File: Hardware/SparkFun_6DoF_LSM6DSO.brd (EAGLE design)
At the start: 25.4 x 25.4 mm, 64 parts, among them J1 QWIIC_RIGHT_ANGLE, J2 QWIIC_RIGHT_ANGLE, U1 LSM6DS0

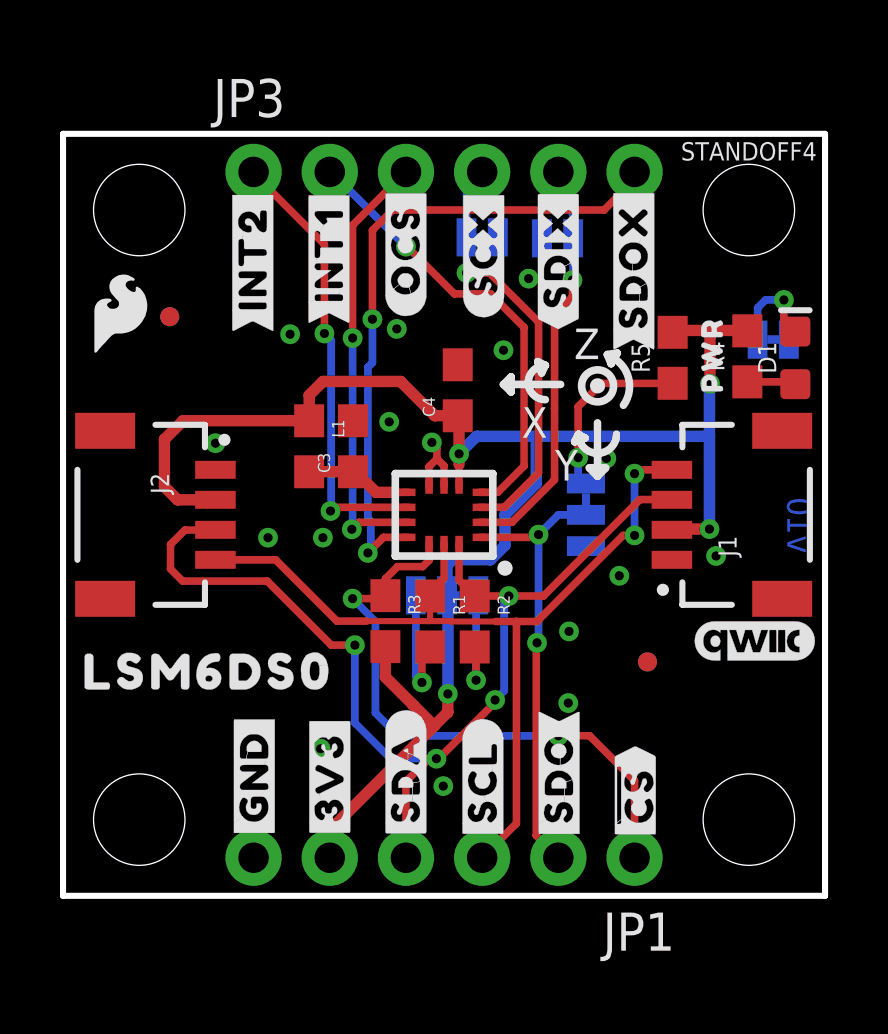
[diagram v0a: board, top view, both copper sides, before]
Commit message: Moves a trace for better ground pour, adds production panel
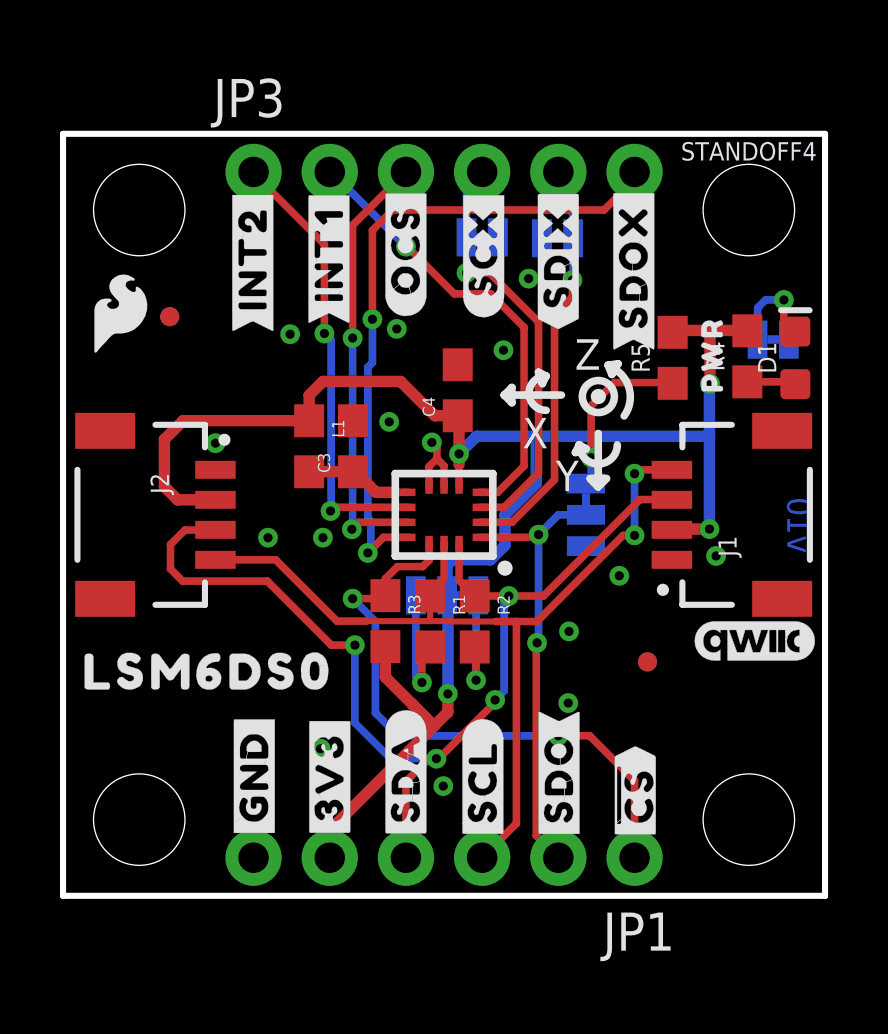
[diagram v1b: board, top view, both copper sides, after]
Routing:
- net GND: vias 16 -> 15
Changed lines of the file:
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@@
 <setting verticaltext="up"/>
 </settings>
-<grid distance="0.05" unitdist="inch" unit="inch" style="dots" multiple="1" display="yes" altdistance="0.005" altunitdist="inch" altunit="inch"/>
+<grid distance="0.01" unitdist="inch" unit="inch" style="dots" multiple="1" display="yes" altdistance="0.001" altunitdist="inch" altunit="inch"/>
 <layers>
 <layer number="1" name="Top" color="4" fill="1" visible="yes" active="yes"/>
@@
 <wire x1="25.4" y1="0" x2="25.4" y2="25.4" width="0.2032" layer="20"/>
 <text x="24.139525" y="11.420475" size="0.8128" layer="16" font="vector" ratio="22" rot="MR90">v10</text>
-<wire x1="14.6812" y1="17.046575" x2="16.5862" y2="17.046575" width="0.254" layer="21"/>
-<wire x1="16.0782" y1="16.538575" x2="16.0782" y2="17.681575" width="0.254" layer="21" curve="-180"/>
-<wire x1="16.0782" y1="17.681575" x2="15.8242" y2="17.808575" width="0.254" layer="21"/>
-<wire x1="16.0782" y1="17.681575" x2="15.9512" y2="17.427575" width="0.254" layer="21"/>
-<wire x1="14.6812" y1="17.046575" x2="14.9352" y2="16.792575" width="0.254" layer="21"/>
-<wire x1="14.6812" y1="17.046575" x2="14.9352" y2="17.300575" width="0.254" layer="21"/>
-<wire x1="17.814925" y1="13.98905" x2="17.814925" y2="15.76705" width="0.254" layer="21"/>
-<wire x1="18.449925" y1="15.38605" x2="17.179925" y2="15.38605" width="0.254" layer="21" curve="-180"/>
-<wire x1="17.179925" y1="15.38605" x2="17.052925" y2="15.13205" width="0.254" layer="21"/>
-<wire x1="17.179925" y1="15.38605" x2="17.408525" y2="15.25905" width="0.254" layer="21"/>
-<wire x1="17.814925" y1="13.98905" x2="18.068925" y2="14.24305" width="0.254" layer="21"/>
-<wire x1="17.814925" y1="13.98905" x2="17.560925" y2="14.24305" width="0.254" layer="21"/>
-<wire x1="18.094325" y1="14.26845" x2="17.535525" y2="14.26845" width="0.254" layer="21"/>
-<wire x1="17.408525" y1="15.25905" x2="17.052925" y2="15.13205" width="0.254" layer="21"/>
-<wire x1="15.8242" y1="17.808575" x2="15.9512" y2="17.427575" width="0.254" layer="21"/>
-<wire x1="14.9352" y1="17.300575" x2="14.9352" y2="16.792575" width="0.254" layer="21"/>
-<text x="16.398875" y="13.843" size="1.016" layer="21" font="vector" ratio="15" rot="SR0">Y</text>
-<text x="15.287625" y="15.27175" size="1.016" layer="21" font="vector" ratio="15" rot="SR0">X</text>
-<text x="17.033875" y="17.891125" size="1.016" layer="21" font="vector" ratio="15" rot="SR0">Z</text>
-<wire x1="18.14195" y1="18.043525" x2="18.475325" y2="18.09115" width="0.254" layer="21"/>
-<wire x1="18.14195" y1="18.043525" x2="18.26895" y2="17.73555" width="0.254" layer="21"/>
-<wire x1="18.26895" y1="17.73555" x2="18.475325" y2="18.09115" width="0.254" layer="21"/>
-<wire x1="18.272125" y1="17.96415" x2="18.678525" y2="16.35125" width="0.254" layer="21" curve="-100"/>
-<circle x="17.8181" y="16.99895" radius="0.127" width="0.254" layer="21"/>
-<circle x="17.8181" y="16.99895" radius="0.5334" width="0.254" layer="21"/>
+<wire x1="14.7066" y1="16.690975" x2="16.6116" y2="16.690975" width="0.254" layer="21"/>
+<wire x1="16.1036" y1="16.182975" x2="16.1036" y2="17.325975" width="0.254" layer="21" curve="-180"/>
+<wire x1="16.1036" y1="17.325975" x2="15.8496" y2="17.452975" width="0.254" layer="21"/>
+<wire x1="16.1036" y1="17.325975" x2="15.9766" y2="17.071975" width="0.254" layer="21"/>
+<wire x1="14.7066" y1="16.690975" x2="14.9606" y2="16.436975" width="0.254" layer="21"/>
+<wire x1="14.7066" y1="16.690975" x2="14.9606" y2="16.944975" width="0.254" layer="21"/>
+<wire x1="17.840325" y1="13.63345" x2="17.840325" y2="15.41145" width="0.254" layer="21"/>
+<wire x1="18.475325" y1="15.03045" x2="17.205325" y2="15.03045" width="0.254" layer="21" curve="-180"/>
+<wire x1="17.205325" y1="15.03045" x2="17.078325" y2="14.77645" width="0.254" layer="21"/>
+<wire x1="17.205325" y1="15.03045" x2="17.433925" y2="14.90345" width="0.254" layer="21"/>
+<wire x1="17.840325" y1="13.63345" x2="18.094325" y2="13.88745" width="0.254" layer="21"/>
+<wire x1="17.840325" y1="13.63345" x2="17.586325" y2="13.88745" width="0.254" layer="21"/>
+<wire x1="18.119725" y1="13.91285" x2="17.560925" y2="13.91285" width="0.254" layer="21"/>
+<wire x1="17.433925" y1="14.90345" x2="17.078325" y2="14.77645" width="0.254" layer="21"/>
+<wire x1="15.8496" y1="17.452975" x2="15.9766" y2="17.071975" width="0.254" layer="21"/>
+<wire x1="14.9606" y1="16.944975" x2="14.9606" y2="16.436975" width="0.254" layer="21"/>
+<text x="16.424275" y="13.4874" size="1.016" layer="21" font="vector" ratio="15" rot="SR0">Y</text>
+<text x="15.313025" y="14.91615" size="1.016" layer="21" font="vector" ratio="15" rot="SR0">X</text>
+<text x="17.059275" y="17.535525" size="1.016" layer="21" font="vector" ratio="15" rot="SR0">Z</text>
+<wire x1="18.16735" y1="17.687925" x2="18.500725" y2="17.73555" width="0.254" layer="21"/>
+<wire x1="18.16735" y1="17.687925" x2="18.29435" y2="17.37995" width="0.254" layer="21"/>
+<wire x1="18.29435" y1="17.37995" x2="18.500725" y2="17.73555" width="0.254" layer="21"/>
+<wire x1="18.297525" y1="17.60855" x2="18.703925" y2="15.99565" width="0.254" layer="21" curve="-100"/>
+<circle x="17.8435" y="16.64335" radius="0.127" width="0.254" layer="21"/>
+<circle x="17.8435" y="16.64335" radius="0.5334" width="0.254" layer="21"/>
 <wire x1="19.116675" y1="9.2948125" x2="21.021675" y2="9.2948125" width="0.254" layer="22"/>
 <wire x1="20.513675" y1="8.7868125" x2="20.513675" y2="9.9298125" width="0.254" layer="22" curve="-180"/>
@@
 <via x="16.8402" y="6.4262" extent="1-16" drill="0.3048"/>
 <via x="16.8656" y="8.8138" extent="1-16" drill="0.3048"/>
-<via x="18.1102" y="14.5796" extent="1-16" drill="0.3048"/>
 </signal>
 <signal name="VDD">
@@
 <wire x1="16.9799" y1="20.5232" x2="16.9799" y2="19.9644" width="0.254" layer="1"/>
 <wire x1="16.9799" y1="19.9644" x2="16.383" y2="19.3675" width="0.254" layer="1"/>
-<wire x1="16.383" y1="19.3675" x2="16.383" y2="16.256" width="0.254" layer="1"/>
-<wire x1="16.383" y1="16.256" x2="16.383" y2="13.8684" width="0.254" layer="1"/>
+<wire x1="16.383" y1="19.3675" x2="16.383" y2="13.8684" width="0.254" layer="1"/>
 <wire x1="17.0053" y1="21.9202" x2="17.0053" y2="22.733" width="0.254" layer="16"/>
 <wire x1="17.0053" y1="22.733" x2="16.51" y2="23.2283" width="0.254" layer="16"/>
@@
 <contactref element="ADDR" pad="3"/>
 <contactref element="R5" pad="1"/>
-<via x="17.1704" y="14.605" extent="1-16" drill="0.3048"/>
-<wire x1="17.1704" y1="14.605" x2="17.1704" y2="16.3068" width="0.254" layer="1"/>
-<wire x1="17.43075" y1="13.7414" x2="17.1704" y2="14.00175" width="0.254" layer="16"/>
-<wire x1="17.1704" y1="14.605" x2="17.1704" y2="14.00175" width="0.254" layer="16"/>
-<wire x1="17.1704" y1="16.3068" x2="17.946" y2="17.0824" width="0.254" layer="1"/>
-<wire x1="17.946" y1="17.0824" x2="20.32" y2="17.0824" width="0.254" layer="1"/>
+<via x="17.6022" y="14.605" extent="1-16" drill="0.3048"/>
+<wire x1="17.6022" y1="14.605" x2="17.6022" y2="16.3322" width="0.254" layer="1"/>
+<wire x1="17.6022" y1="14.605" x2="17.6022" y2="13.91285" width="0.254" layer="16"/>
+<wire x1="17.43075" y1="13.7414" x2="17.6022" y2="13.91285" width="0.254" layer="16"/>
+<wire x1="17.6022" y1="16.3322" x2="18.3778" y2="17.1078" width="0.254" layer="1"/>
+<wire x1="20.2946" y1="17.1078" x2="18.3778" y2="17.1078" width="0.254" layer="1"/>
+<wire x1="20.2946" y1="17.1078" x2="20.32" y2="17.0824" width="0.254" layer="1"/>
 </signal>
 <signal name="SDO_AUX">

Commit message: Adds red LED with PROD_ID to schematic
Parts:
- D1: value (none) -> RED
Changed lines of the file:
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@@
 <setting verticaltext="up"/>
 </settings>
-<grid distance="0.01" unitdist="inch" unit="inch" style="dots" multiple="1" display="yes" altdistance="0.001" altunitdist="inch" altunit="inch"/>
+<grid distance="0.05" unitdist="inch" unit="inch" style="dots" multiple="1" display="yes" altdistance="0.005" altunitdist="inch" altunit="inch"/>
 <layers>
 <layer number="1" name="Top" color="4" fill="1" visible="yes" active="yes"/>
@@
 <attribute name="VALUE" x="1.778" y="14.351" size="0.6096" layer="27" font="vector" ratio="20" rot="R270"/>
 </element>
-<element name="D1" library="SparkFun-LED" package="LED-0603" value="" x="24.4094" y="17.9324" smashed="yes" rot="R90">
+<element name="D1" library="SparkFun-LED" package="LED-0603" value="RED" x="24.4094" y="17.9324" smashed="yes" rot="R90">
 <attribute name="NAME" x="23.7744" y="17.9324" size="0.6096" layer="25" font="vector" ratio="20" rot="R90" align="bottom-center"/>
-<attribute name="VALUE" x="25.0444" y="17.9324" size="0.6096" layer="27" font="vector" ratio="20" rot="R90" align="top-center"/>
+<attribute name="PROD_ID" value="DIO-00819" x="24.4094" y="17.9324" size="1.778" layer="27" rot="R90" display="off"/>
+<attribute name="VALUE" value="RED" x="25.0444" y="17.9324" size="0.6096" layer="27" font="vector" ratio="20" rot="R90" align="top-center"/>
 </element>
 <element name="R4" library="SparkFun-Resistors" package="0603" value="1k" x="22.8092" y="17.9832" smashed="yes" rot="R90">

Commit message: Removes temp library and uses LSM6DSO IC from SparkFun Eagle Libraries.
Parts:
- U1: device temp:LGA14L -> SparkFun-Sensors:LGA14L
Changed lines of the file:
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@@
 <element name="U$25" library="bot" package="#I2C#11" value="" x="12.827" y="8.4582" smashed="yes" rot="MR0"/>
 <element name="U$28" library="top" package="PWR8" value="" x="21.6408" y="18.034" smashed="yes" rot="R90"/>
-<element name="U1" library="temp" package="LGA14L" value="LSM6DS0" x="12.7" y="12.7" smashed="yes" rot="R180">
+<element name="U1" library="SparkFun-Sensors" package="LGA14L" value="LSM6DS0" x="12.7" y="12.7" smashed="yes" rot="R180">
 <attribute name="NAME" x="14.057" y="10.928" size="0.6096" layer="27" font="vector" ratio="20" rot="R180"/>
 <attribute name="PROD_ID" value="IC-15837" x="12.7" y="12.7" size="1.778" layer="27" rot="R180" display="off"/>
